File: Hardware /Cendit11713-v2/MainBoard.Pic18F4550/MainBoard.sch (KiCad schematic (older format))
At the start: 37 parts, among them CON2 USB_CON, J1 RESET_CON

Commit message: En CendiLab edicion de archivo UI + Respaldo
    - Edicion de fxl para setup
    - Respaldo de archivos esquematicos + PCB
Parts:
- removed CON2: USB_CON, symbol USB_CON
- removed JP1: Jumper, symbol Jumper
- added CON?: USB_CON, symbol USB_CON
- added R? (x2): 4.7K, symbol R_Small
- JP?: value Jumper_NO_Small -> JMP3V
- JP?: value Jumper_NC_Small -> JMP5V
- L1: value Choke -> FERRITE_BEAD
- L2: value USB_CHOKE -> FERRITE_BEAD
- R5, R?: value 100R -> 1.5K
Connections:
- net labels added: SCK, SDA, VUSB, VUSB_CAP
- wire segments 100 -> 128
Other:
- moved on the sheet: C?, CON?, JP?, L1, L2, R?, U?

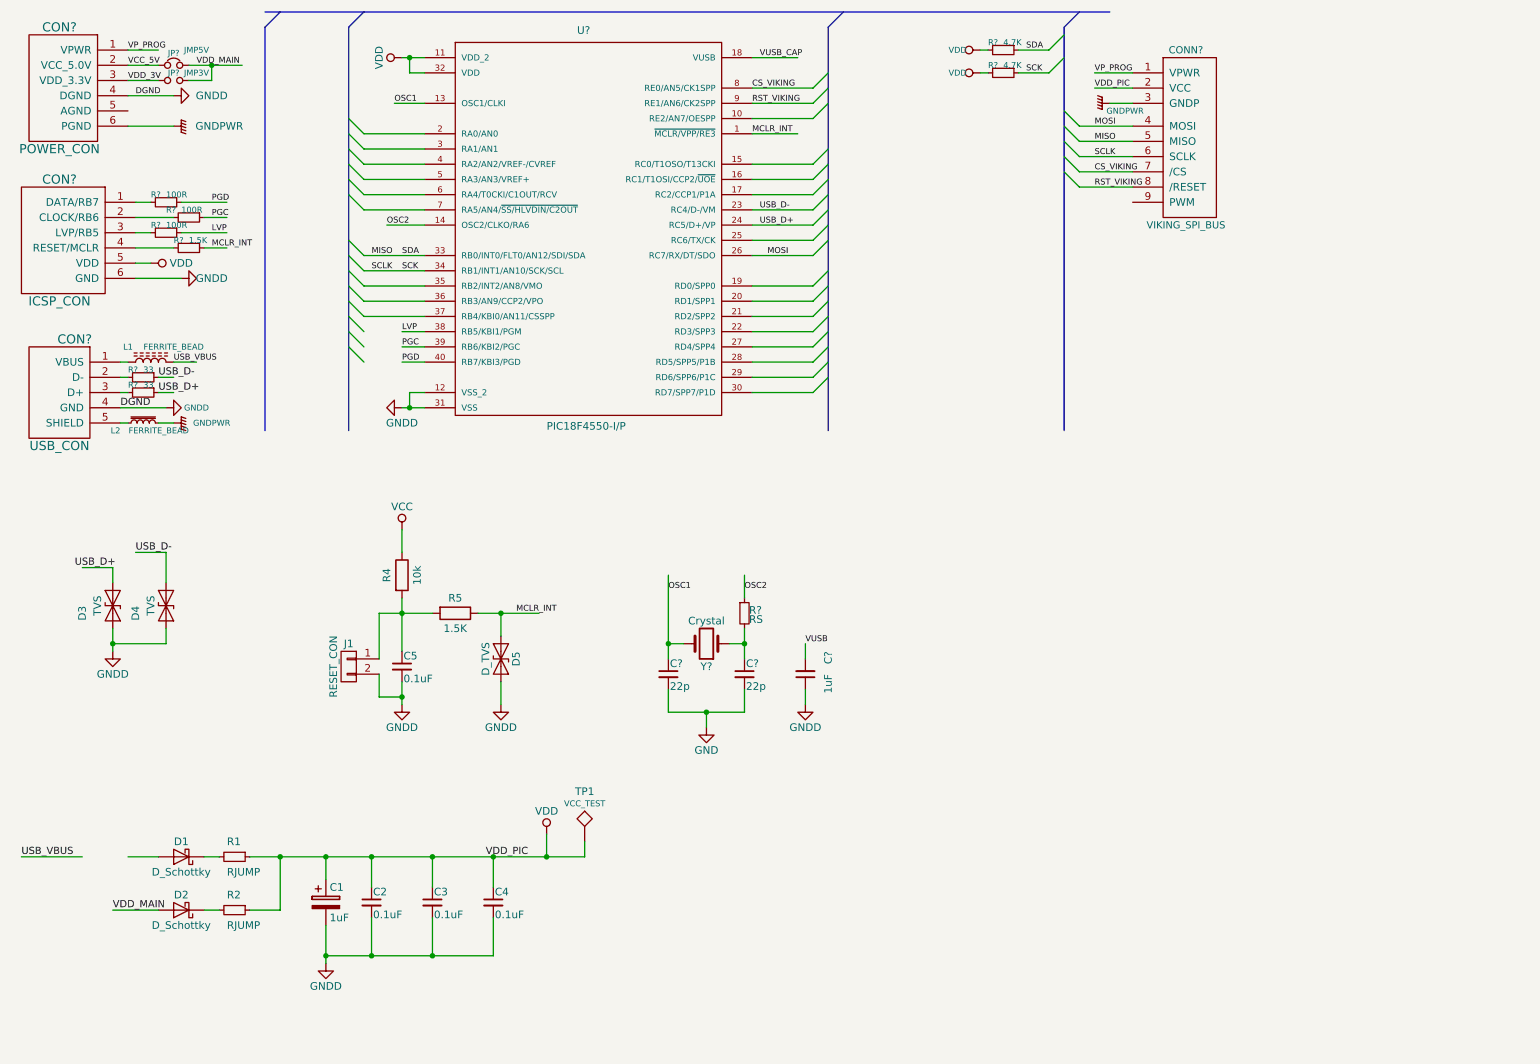
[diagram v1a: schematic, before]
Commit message: En Cendit11713 edicion de esquematicos + revision PCBs
  - Edicion de esquematicos tarjeta madre
  - Revision de PCBs corrección de footprints
  - Descarga de footprints + creacion lib simbolos: RTC + sensor temp/hum
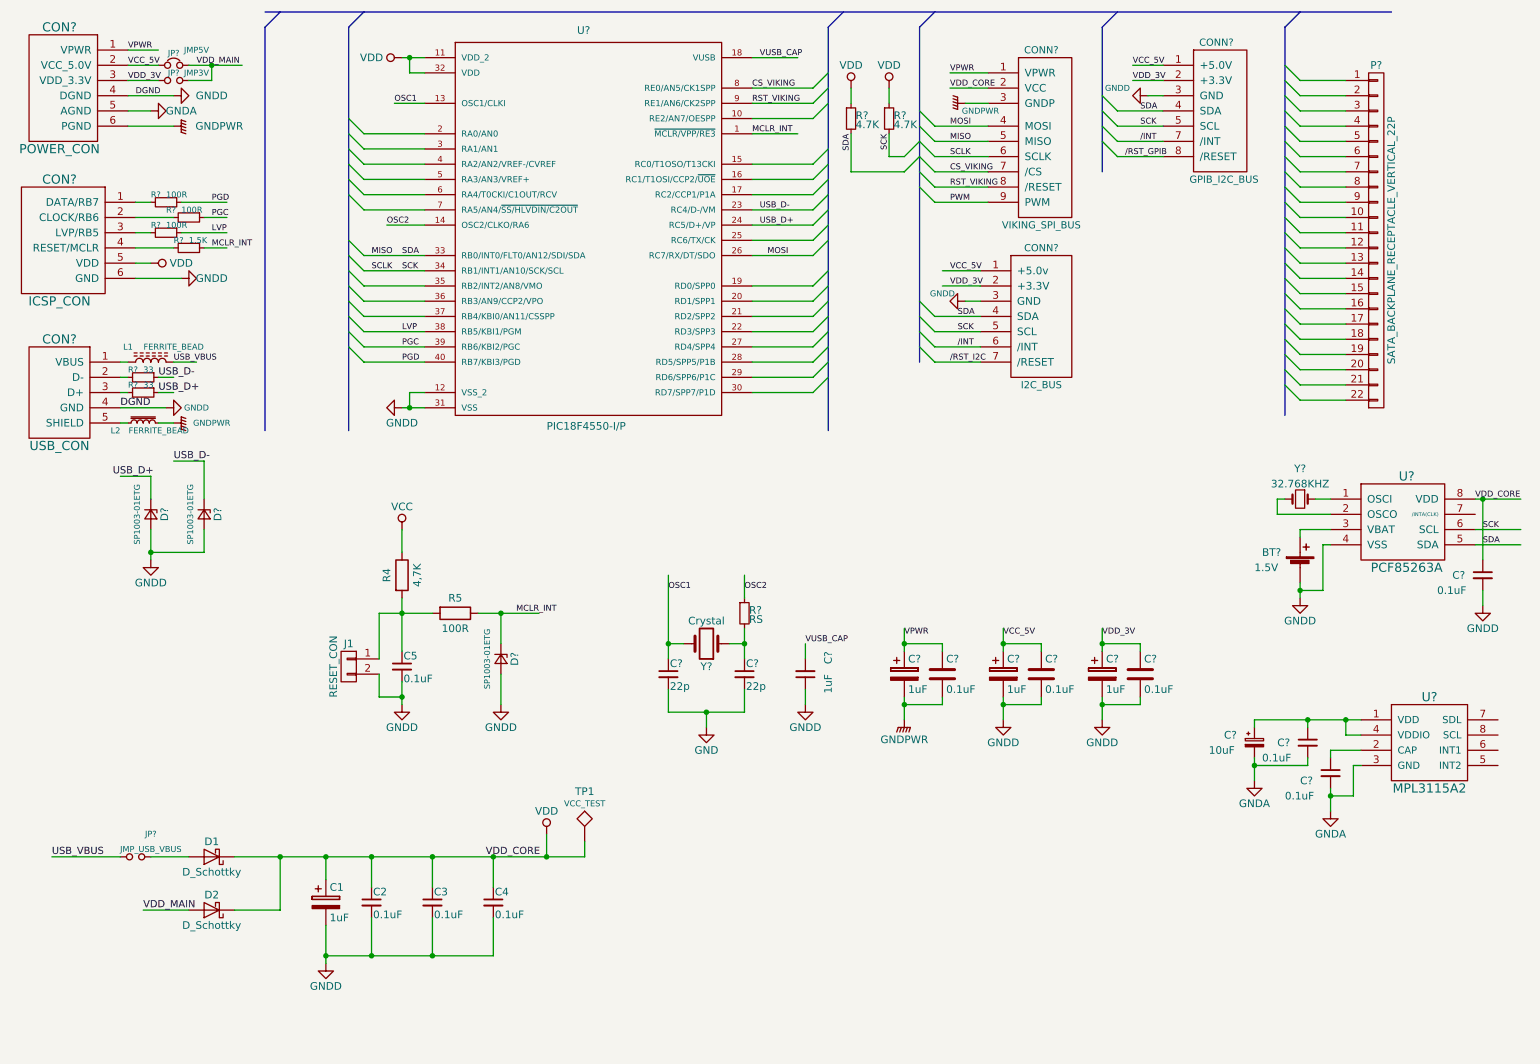
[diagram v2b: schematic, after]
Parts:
- removed CON?: POWER_CON, symbol POWER_CON
- removed D3, D4: TVS, symbol D_TVS
- removed D5: D_TVS, symbol D_TVS
- removed R1, R2: RJUMP, symbol R_Small
- removed R? (x2): 4.7K, symbol R_Small
- added BT?: 1.5V, symbol Battery_Cell
- added C? (x3): 0.1uF, symbol C_Small
- added C?: 10uF, symbol CP_Small
- added C? (x3): 1uF, symbol CP
- added C? (x3): 0.1uF, symbol C
- added CON?: POWER_CON, symbol POWER_CON
- added CONN?: GPIB_I2C_BUS, symbol GPIB_I2C_BUS
- added CONN?: I2C_BUS, symbol I2C_BUS
- added D? (x3): SP1003-01ETG, symbol D_Zener_Small
- added JP?: JMP_USB_VBUS, symbol Jumper_NO_Small
- added P?: SATA_BACKPLANE_RECEPTACLE_VERTICAL_22P, symbol CONN_01X22
- added R? (x2): 4.7K, symbol R_Small
- added U?: PCF85263A, symbol PCF85263A
- added U?: MPL3115A2, symbol MPL3115A2
- added Y?: 32.768KHZ, symbol Crystal_Small
- R4: value 10k -> 4,7K
- R5: value 1.5K -> 100R
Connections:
- net labels added: /INT, /RST_GPIB, /RST_I2C, GNDA, PWM, VDD_CORE, VPWR
- net labels removed: VDD_PIC, VP_PROG, VUSB
- wire segments 128 -> 213
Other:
- moved on the sheet: CONN?, D1, D2
